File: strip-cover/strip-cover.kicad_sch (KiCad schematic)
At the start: 7 parts

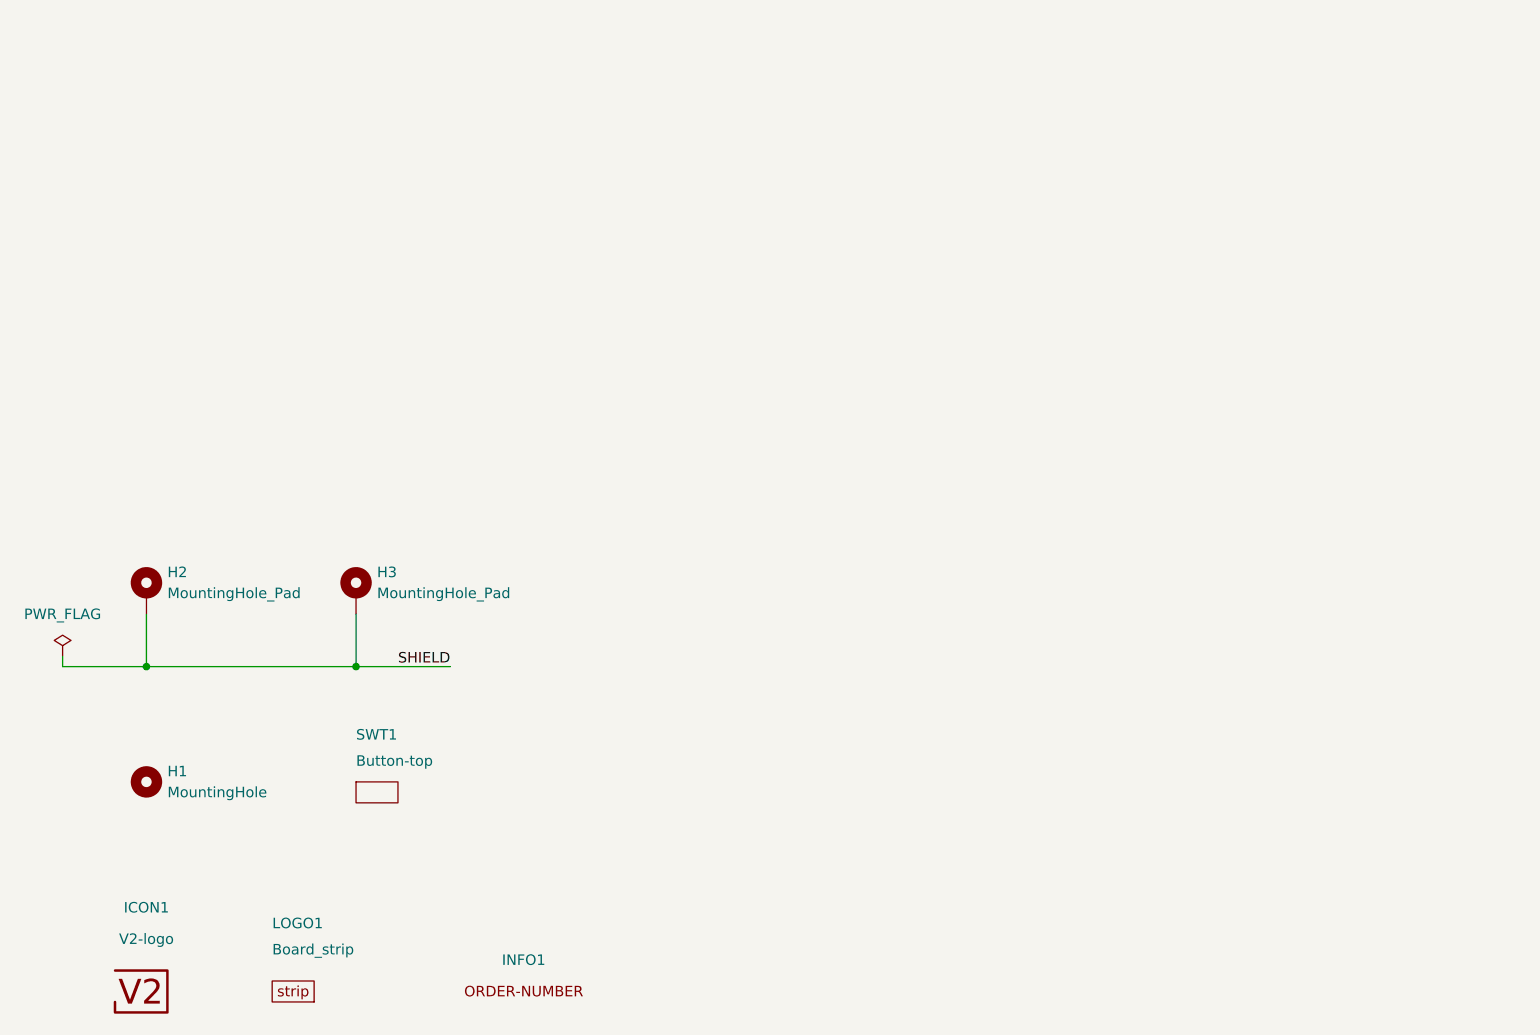
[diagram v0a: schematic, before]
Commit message: Update to KiCad 7.0
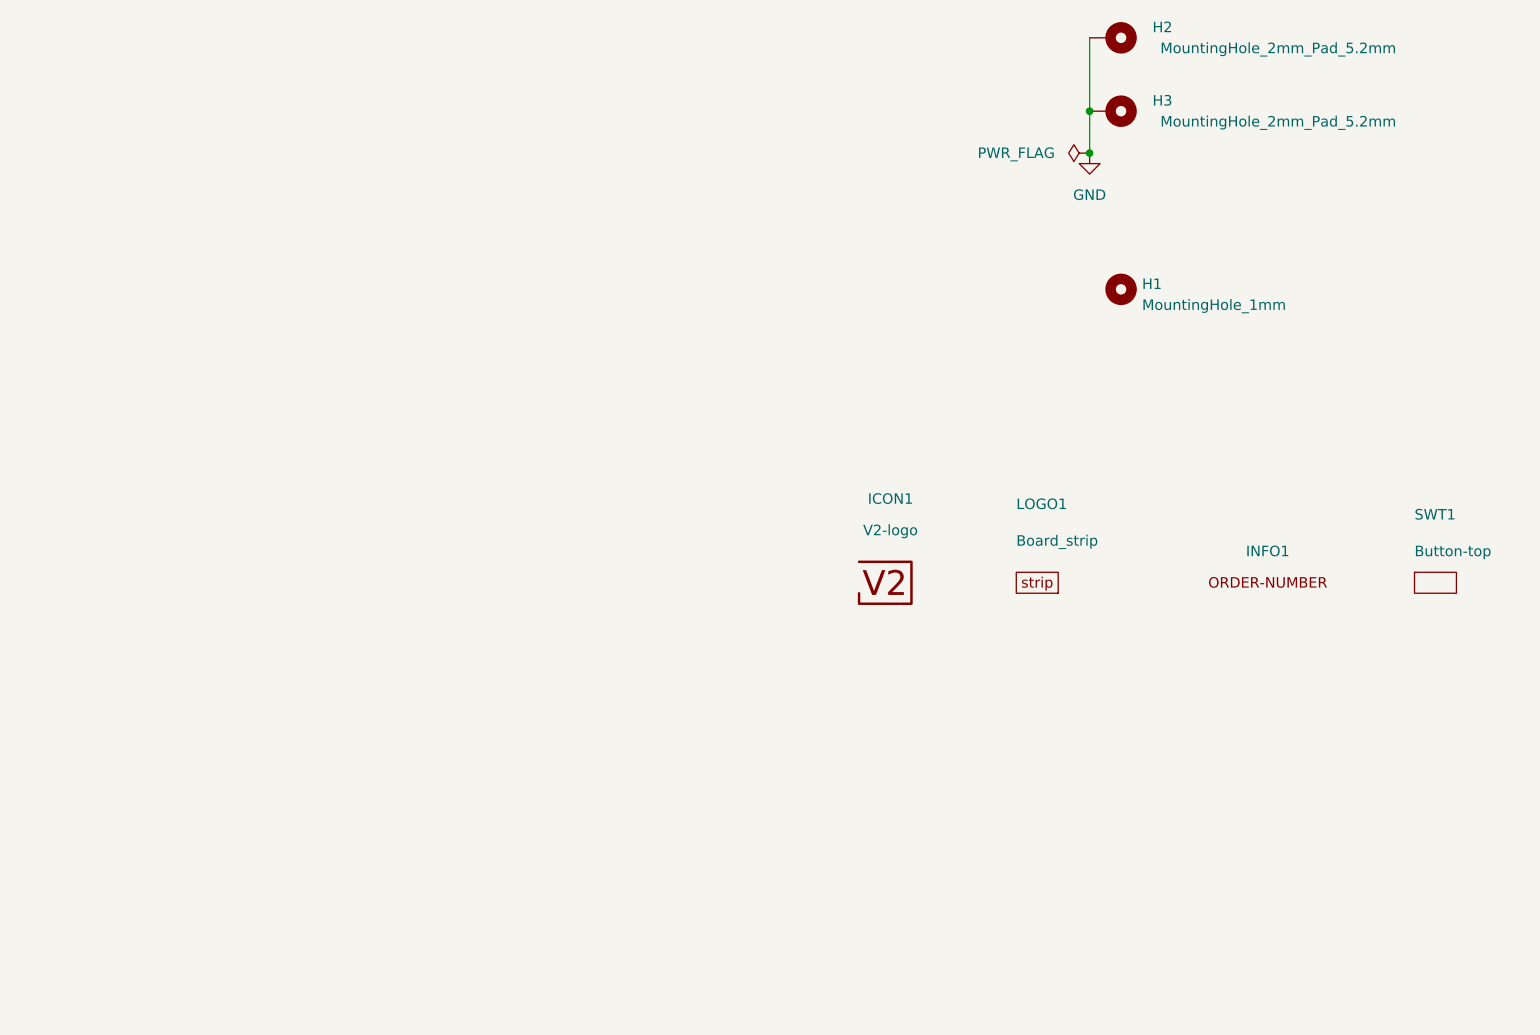
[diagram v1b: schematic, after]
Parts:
- H1: value MountingHole -> MountingHole_1mm; footprint V2_Mechanical:Mounting_Hole_1 -> V2_Mechanical:MountingHole_1mm; symbol Mechanical:MountingHole -> V2_Mechanical:MountingHole_1mm
- H2, H3: value MountingHole_Pad -> MountingHole_2mm_Pad_5.2mm; footprint V2_Mechanical:Mounting_Hole_Pad_2-5.2 -> V2_Mechanical:Mounting_Hole_2mm_Pad_5.2mm; symbol Mechanical:MountingHole_Pad -> V2_Mechanical:MountingHole_2mm_Pad_5.2mm
- INFO1: value ORDER-NUMBER -> Order_Number
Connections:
- net SHIELD renamed GND
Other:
- title: V2 strip Cover -> V2 strip
- moved on the sheet: H1, H2, H3, ICON1, INFO1, LOGO1, SWT1

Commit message: Refresh
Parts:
- H1: now left out of the parts list
- H2, H3: footprint V2_Mechanical:Mounting_Hole_2mm_Pad_5.2mm -> V2_Mechanical:MountingHole_2mm_Pad_5.2mm; now left out of the parts list
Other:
- moved on the sheet: ICON1
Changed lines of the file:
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@@
-(kicad_sch (version 20221206) (generator eeschema)
+(kicad_sch (version 20230121) (generator eeschema)
   (paper "A4")
   (title_block
     (title "V2 strip")
-    (date "2023-01-09")
+    (date "2023-09-12")
     (rev "2")
     (company "Versio Duo")
@@
       (effects (font (size 1.27 1.27)) hide)
     )
+    (property "Sim.Enable" "0" (at 140.97 133.35 0)
+      (effects (font (size 1.27 1.27)) hide)
+    )
     (instances
       (project "strip-cover"
@@
       (effects (font (size 1.27 1.27)) hide)
     )
+    (property "Sim.Enable" "0" (at 168.91 133.35 0)
+      (effects (font (size 1.27 1.27)) hide)
+    )
     (instances
       (project "strip-cover"
@@
       (effects (font (size 1.27 1.27)) hide)
     )
+    (property "Sim.Enable" "0" (at 189.23 133.35 0)
+      (effects (font (size 1.27 1.27)) hide)
+    )
     (instances
       (project "strip-cover"
@@
   )
   (symbol (lib_id "V2_Mechanical:MountingHole_2mm_Pad_5.2mm") (at 149.86 67.31 270) (unit 1)
-    (in_bom yes) (on_board yes) (dnp no)
+    (in_bom no) (on_board yes) (dnp no)
     (property "Reference" "H2" (at 154.94 66.04 90)
       (effects (font (size 1.27 1.27)) (justify left))
@@
       (effects (font (size 1.27 1.27)))
     )
-    (property "Footprint" "V2_Mechanical:Mounting_Hole_2mm_Pad_5.2mm" (at 139.7 67.31 0)
+    (property "Footprint" "V2_Mechanical:MountingHole_2mm_Pad_5.2mm" (at 139.7 67.31 0)
       (effects (font (size 1.27 1.27)) hide)
     )
     (property "Datasheet" "~" (at 149.86 67.31 0)
+      (effects (font (size 1.27 1.27)) hide)
+    )
+    (property "Sim.Enable" "0" (at 149.86 67.31 0)
       (effects (font (size 1.27 1.27)) hide)
     )
@@
   )
   (symbol (lib_id "V2_Mechanical:MountingHole_1mm") (at 151.13 97.79 0) (unit 1)
-    (in_bom yes) (on_board yes) (dnp no) (fields_autoplaced)
+    (in_bom no) (on_board yes) (dnp no) (fields_autoplaced)
     (property "Reference" "H1" (at 153.67 97.155 0)
       (effects (font (size 1.27 1.27)) (justify left))
@@
     )
     (property "Datasheet" "~" (at 151.13 97.79 0)
+      (effects (font (size 1.27 1.27)) hide)
+    )
+    (property "Sim.Enable" "0" (at 151.13 97.79 0)
       (effects (font (size 1.27 1.27)) hide)
     )
@@
       (effects (font (size 1.27 1.27)) hide)
     )
+    (property "Sim.Enable" "0" (at 123.19 132.08 0)
+      (effects (font (size 1.27 1.27)) hide)
+    )
     (instances
       (project "strip-cover"
@@
   )
   (symbol (lib_id "V2_Mechanical:MountingHole_2mm_Pad_5.2mm") (at 149.86 76.2 270) (unit 1)
-    (in_bom yes) (on_board yes) (dnp no)
+    (in_bom no) (on_board yes) (dnp no)
     (property "Reference" "H3" (at 154.94 74.93 90)
       (effects (font (size 1.27 1.27)) (justify left))
@@
       (effects (font (size 1.27 1.27)))
     )
-    (property "Footprint" "V2_Mechanical:Mounting_Hole_2mm_Pad_5.2mm" (at 139.7 76.2 0)
+    (property "Footprint" "V2_Mechanical:MountingHole_2mm_Pad_5.2mm" (at 139.7 76.2 0)
       (effects (font (size 1.27 1.27)) hide)
     )
@@
       (effects (font (size 1.27 1.27)) hide)
     )
+    (property "Sim.Enable" "0" (at 149.86 76.2 0)
+      (effects (font (size 1.27 1.27)) hide)
+    )
